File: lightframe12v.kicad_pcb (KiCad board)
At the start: 2 copper layers, 91.4 x 45.7 mm, 47 parts, among them J1 PJ-077, J2 Conn_01x07_Female, J4 Conn_01x07_Female, J5 Conn_01x04_Female, J6 Conn_01x4_Female, Q1 MMBT2222A-TP, Q2 MMBT2222A-TP, SW1 SW_Push, SW2 SW_Push, U1 TPS562211, U2 ESP32-WROOM-32U, U3 TLC5971

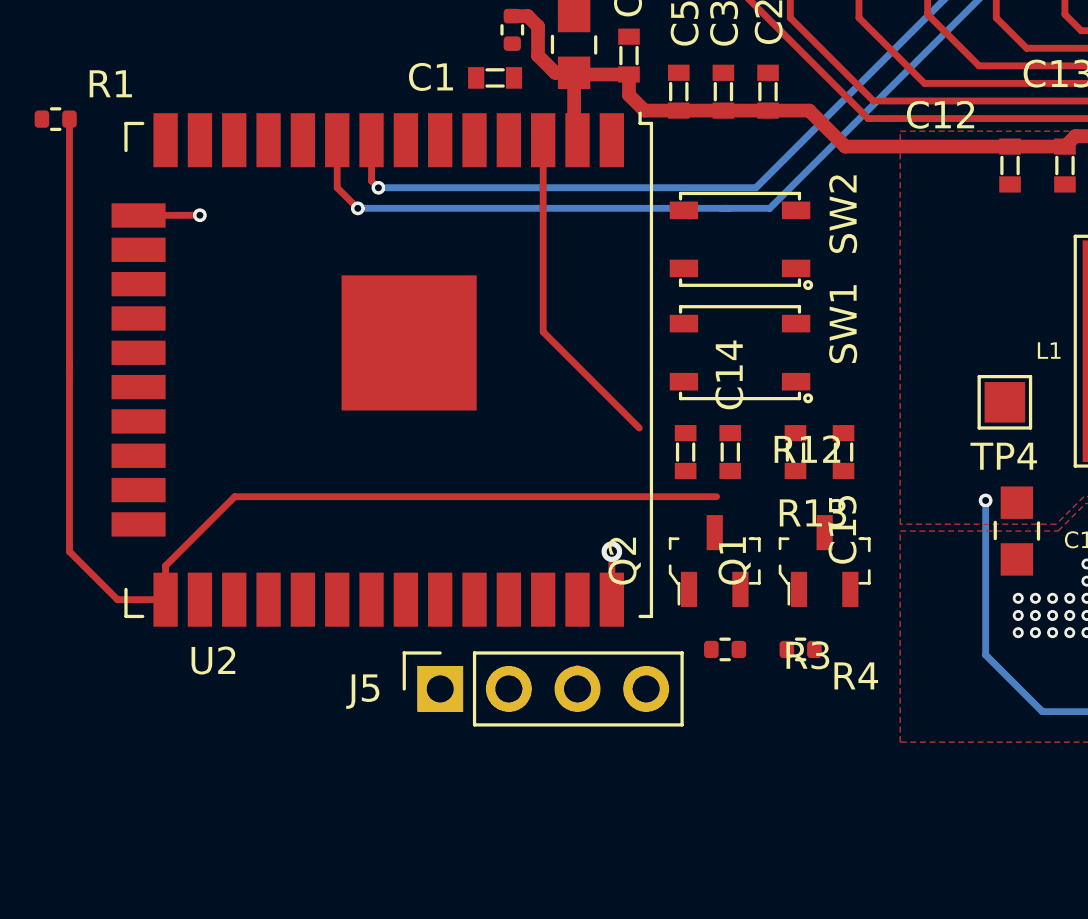
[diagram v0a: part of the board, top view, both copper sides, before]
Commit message: Connecting reset and gpio0.
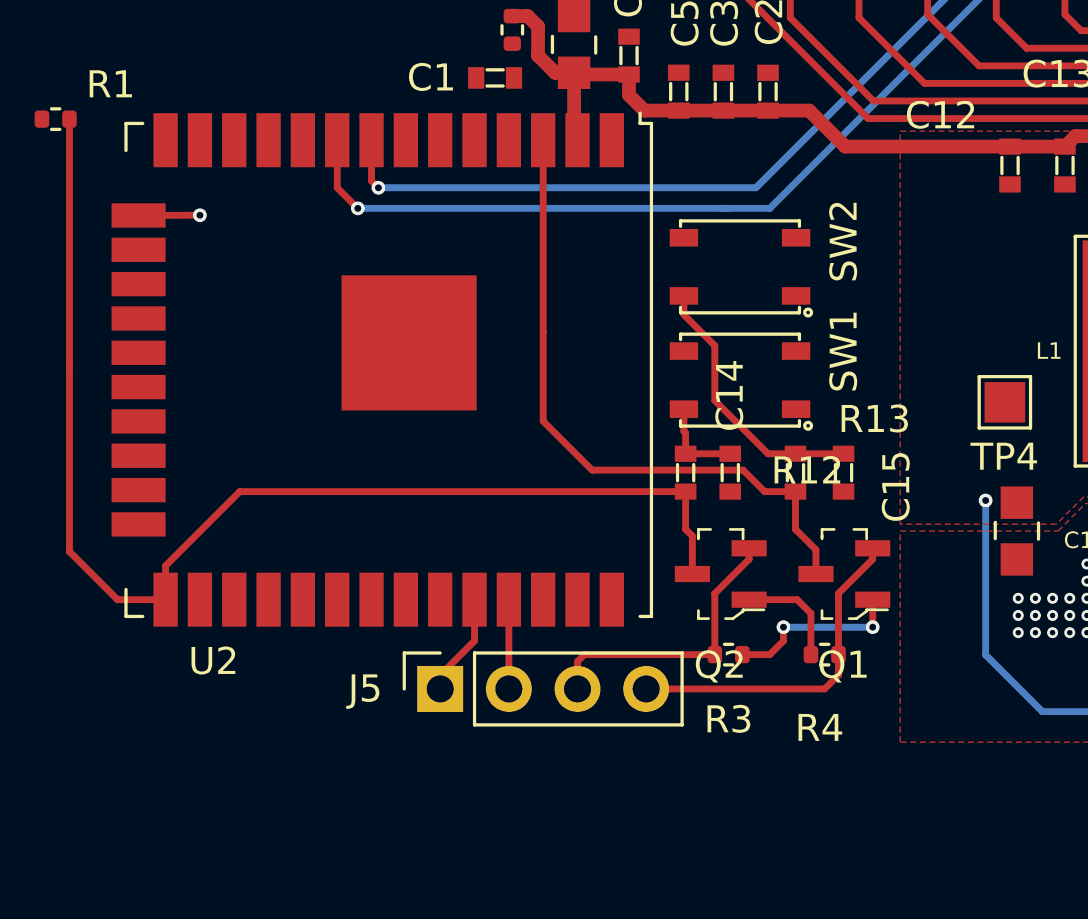
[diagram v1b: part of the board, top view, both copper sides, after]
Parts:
- moved SW2 1.02 mm to (318.9, -523.4)
- moved SW1 1.02 mm to (318.9, -519.2)
- moved R4 0.91 mm to (322.1, -509.0)
- moved Q1 0.87 mm to (322.8, -512.0), turned to 180 degrees
- moved C14 0.76 mm to (318.6, -515.7)
- moved C15 0.76 mm to (322.8, -515.7)
- moved R12 0.76 mm to (316.9, -515.7)
- moved R13 0.76 mm to (321.0, -515.7)
- moved Q2 0.53 mm to (318.2, -512.0), turned to 180 degrees
- moved R3 0.23 mm to (318.5, -509.0)
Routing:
- net /Rts: track 0.00 -> 12.5 mm
- net /Reset: track 12.6 -> 24.6 mm
- net Net-(C15-Pad2): track 0.00 -> 9.92 mm
- net /Dtr: track 0.76 -> 10.7 mm
- net Net-(Q1-Pad1): track 0.00 -> 6.56 mm, vias 0 -> 2
- net Net-(Q2-Pad1): track 0.00 -> 4.02 mm
- net Net-(C14-Pad2): track 0.00 -> 3.33 mm
- net /Rxd: track 0.51 -> 3.83 mm
- net /Txd: track 0.00 -> 3.30 mm
- net /Gpio0: track 43.0 -> 45.1 mm
- net GND: track 6.10 -> 4.32 mm, vias 72 -> 71

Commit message: More routing.
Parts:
- moved R1 23.7 mm to (317.2, -527.6), turned to 270 degrees
- moved T12V 14.7 mm to (355.9, -527.2)
- moved J6 4.13 mm to (299.7, -537.0)
- moved TPG 3.81 mm to (356.1, -508.4)
- moved T3V3 3.78 mm to (327.7, -522.0)
- moved J1 2.87 mm to (354.2, -521.6)
- moved TGND 2.29 mm to (356.1, -511.8)
- moved SW1 2.16 mm to (321.1, -519.2)
- moved SW2 2.16 mm to (321.1, -523.4)
- moved R13 1.53 mm to (322.4, -516.4), turned to 180 degrees
- moved R6 1.48 mm to (314.2, -534.4)
- moved R12 1.20 mm to (317.9, -516.4), turned to 180 degrees
- moved C15 1.06 mm to (323.3, -514.9), turned to 0 degrees
- moved C14 0.92 mm to (318.8, -514.9), turned to 0 degrees
- moved C12 0.76 mm to (328.9, -526.4)
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- renumbered TP1 to T12V, TP4 to T3V3, TP2 to TGND, TP3 to TPG
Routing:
- net /LED1: track 0.00 -> 21.0 mm
- net GND: track 4.32 -> 23.0 mm, vias 71 -> 85
- net /LED2: track 0.00 -> 18.1 mm
- net +12V: track 5.57 -> 21.7 mm, vias 1 -> 2
- net /LED3: track 0.00 -> 15.1 mm
- net /LED4: track 0.00 -> 12.3 mm
- net /Gpio35: track 0.00 -> 9.64 mm
- net /LED5: track 0.00 -> 9.50 mm
- net /Gpio26: track 0.53 -> 9.75 mm
- net /Gpio34: track 0.00 -> 9.12 mm
- net /Gpio27: track 0.00 -> 9.12 mm
- net /Gpio0: track 45.1 -> 36.3 mm
- net /LED6: track 0.00 -> 6.54 mm
- net /Reset: track 24.6 -> 29.4 mm, vias 0 -> 2
- net Net-(R7-Pad2): track 13.9 -> 17.8 mm
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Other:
- board size 91.4 x 45.7 mm -> 64.8 x 35.6 mm
- board text added: "Dtr"
- board text added: "RESET"
- board text added: "Rts"
- board text added: "Rx"
- board text added: "Tx"
- board text added: "ZERO"

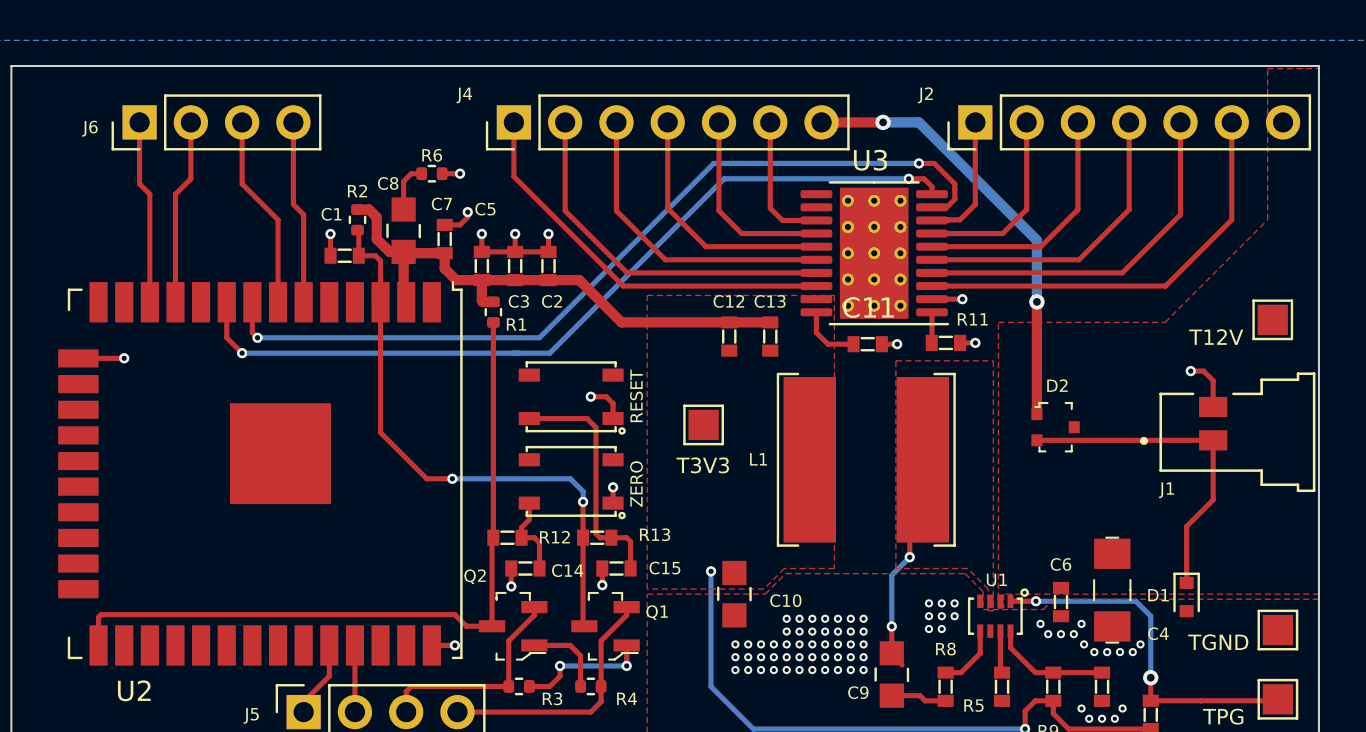
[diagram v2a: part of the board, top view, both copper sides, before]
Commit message: Fixes DRC errors.
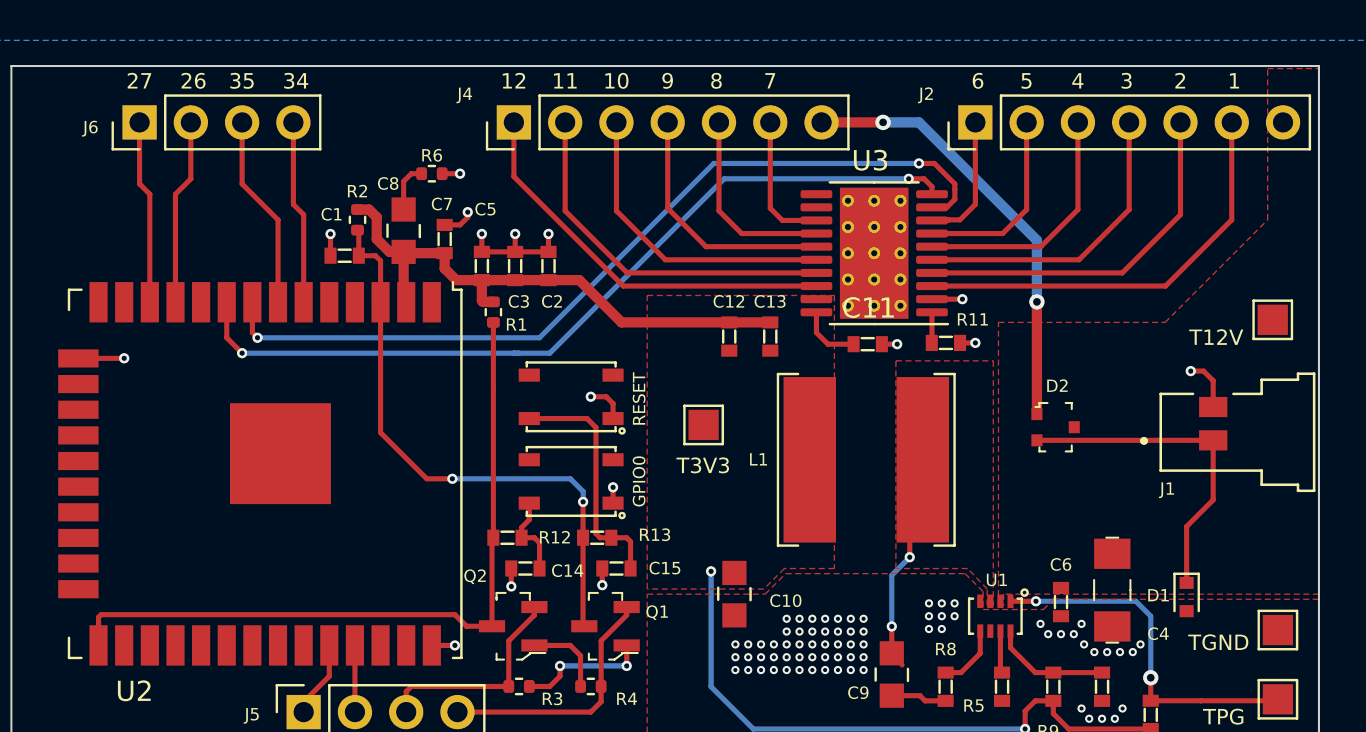
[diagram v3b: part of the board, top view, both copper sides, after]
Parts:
- renumbered SW1 to GPIO0, SW2 to RESET
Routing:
- net (no net): track 0.79 -> 0.00 mm
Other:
- board text added: "1"
- board text added: "10"
- board text added: "11"
- board text added: "12"
- board text added: "2"
- board text added: "26"
- board text added: "27"
- board text added: "3"
- board text added: "34"
- board text added: "35"
- board text added: "4"
- board text added: "5"
- board text added: "6"
- board text added: "7"
- board text added: "8"
- board text added: "9"
- board text removed: "RESET"
- board text removed: "ZERO"

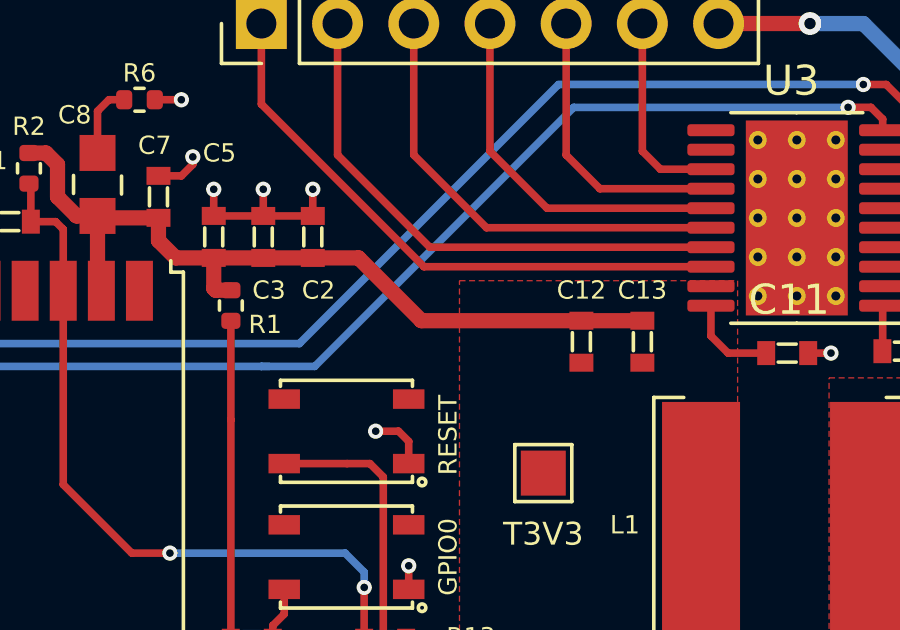
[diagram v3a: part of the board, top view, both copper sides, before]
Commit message: Removes extra thermal pin.
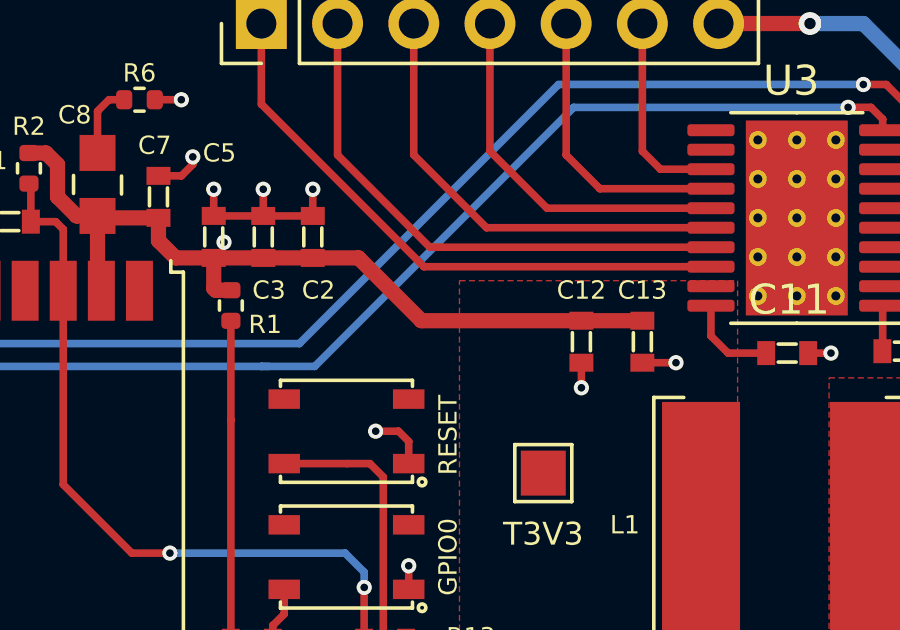
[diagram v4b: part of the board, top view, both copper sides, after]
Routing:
- net GND: track 23.0 -> 25.0 mm, vias 85 -> 87
- net +12V: vias 2 -> 3
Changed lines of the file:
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@@
     (thickness 1.6)
     (drawings 24)
-    (tracks 368)
+    (tracks 375)
     (zones 0)
     (modules 47)
@@
   (segment (start 351.79 -524.637) (end 351.79 -524.637) (width 0.254) (layer F.Cu) (net 1))
   (via (at 351.79 -524.637) (size 0.508) (drill 0.254) (layers F.Cu B.Cu) (net 1))
+  (segment (start 328.93 -525.65) (end 328.93 -524.8148) (width 0.254) (layer F.Cu) (net 1))
+  (segment (start 328.93 -524.8148) (end 328.93 -524.8148) (width 0.254) (layer F.Cu) (net 1))
+  (via (at 328.93 -524.8148) (size 0.508) (drill 0.254) (layers F.Cu B.Cu) (net 1))
+  (segment (start 330.962 -525.65) (end 332.0826 -525.65) (width 0.254) (layer F.Cu) (net 1))
+  (segment (start 332.0826 -525.65) (end 332.0826 -525.65) (width 0.254) (layer F.Cu) (net 1))
+  (via (at 332.0826 -525.65) (size 0.508) (drill 0.254) (layers F.Cu B.Cu) (net 1))
   (segment (start 310.642 -532.64) (end 310.64 -532.638) (width 0.508) (layer F.Cu) (net 2))
   (via (at 343.5858 -506.9078) (size 0.508) (drill 0.254) (layers F.Cu B.Cu) (net 2))
@@
   (segment (start 344.17 -531.114) (end 338.328 -536.956) (width 0.508) (layer B.Cu) (net 33))
   (segment (start 344.17 -528.066) (end 344.17 -531.114) (width 0.508) (layer B.Cu) (net 33))
+  (via (at 317.0174 -529.6662) (size 0.508) (drill 0.254) (layers F.Cu B.Cu) (net 33))
   (segment (start 312.801 -532.6425) (end 312.801 -534.035) (width 0.254) (layer F.Cu) (net 34))
   (segment (start 313.182 -534.416) (end 313.69 -534.416) (width 0.254) (layer F.Cu) (net 34))

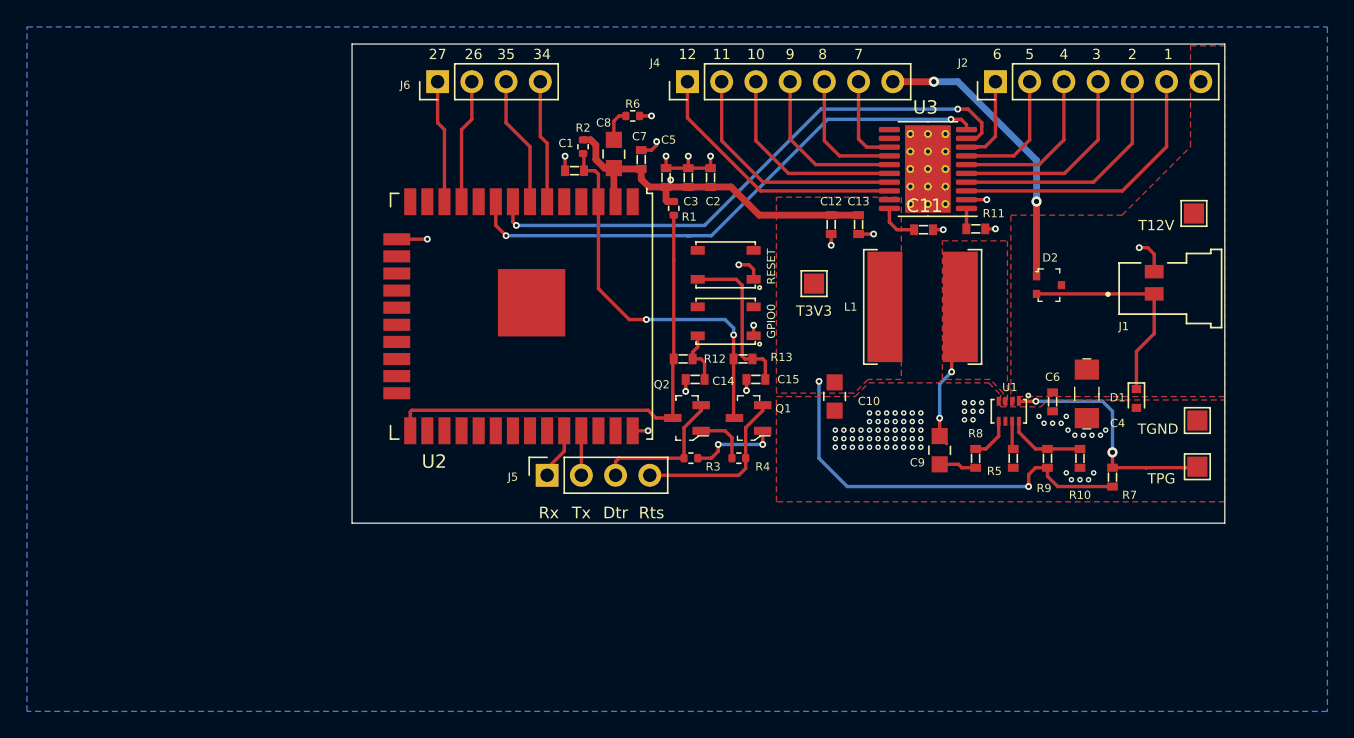
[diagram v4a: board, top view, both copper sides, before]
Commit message: Fiducials and mount points.
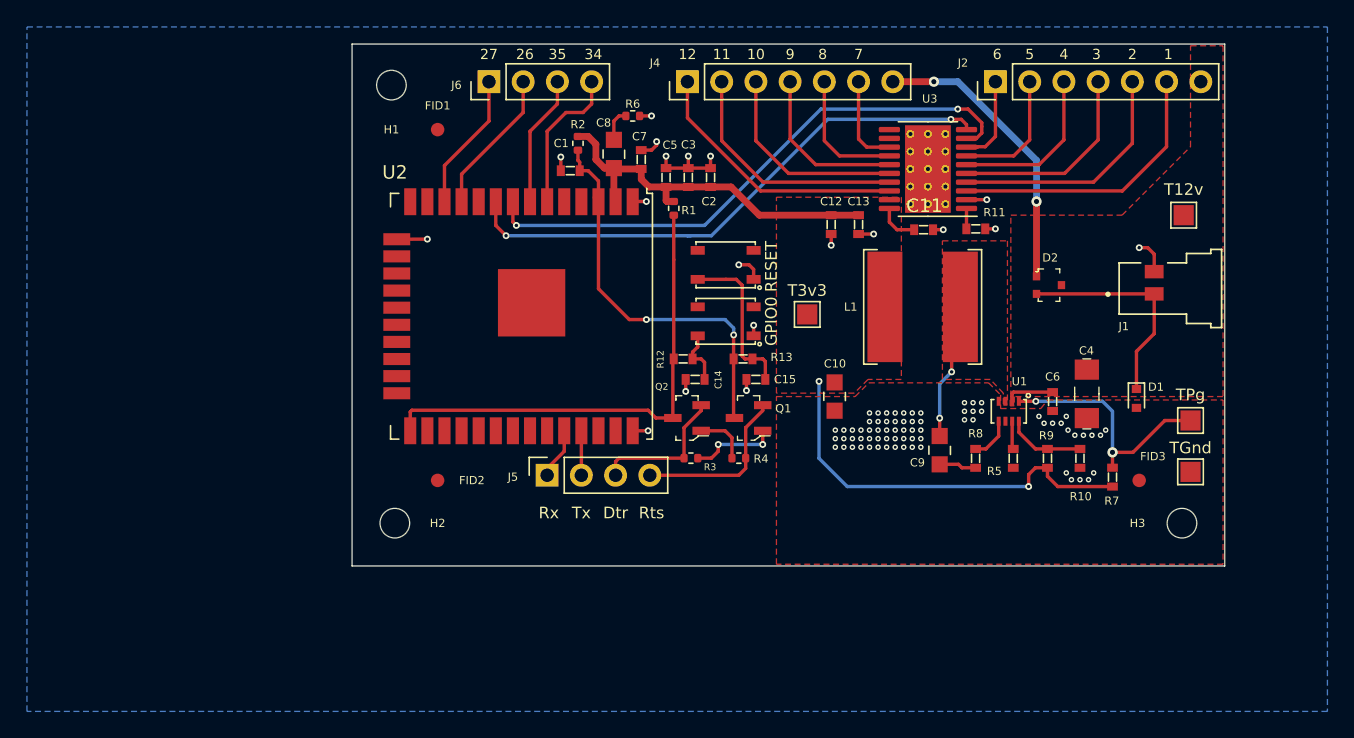
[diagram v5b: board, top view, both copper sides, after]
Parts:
- added FID1: Fiducial, Fiducial:Fiducial_1mm_Mask2mm, F.Cu at (299.7, -533.4)
- added FID2: Fiducial, Fiducial:Fiducial_1mm_Mask2mm, F.Cu at (299.7, -507.4)
- added FID3: Fiducial, Fiducial:Fiducial_1mm_Mask2mm, F.Cu at (351.8, -507.4)
- added H1: TopLeft, MountingHole:MountingHole_2.2mm_M2, F.Cu at (296.3, -536.7)
- added H2: BottomLeft, MountingHole:MountingHole_2.2mm_M2, F.Cu at (296.5, -504.2)
- added H3: TopRight, MountingHole:MountingHole_2.2mm_M2, F.Cu at (355.0, -504.2)
- moved TP2 3.84 mm to (355.6, -508.0)
- moved J6 3.81 mm to (303.5, -537.0)
- moved TP3 3.47 mm to (355.6, -511.8)
- moved TP4 2.34 mm to (327.2, -519.7)
- moved TP1 0.77 mm to (355.1, -527.0)
- moved R2 0.46 mm to (310.1, -532.4)
- moved C1 0.31 mm to (309.6, -530.4)
- renumbered GPIO0 to SW1, RESET to SW2, T12V to TP1, TGND to TP2, TPG to TP3, T3V3 to TP4
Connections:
- U2 pad 39: GND -> (no net)
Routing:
- net +12V: track 21.7 -> 25.3 mm, vias 3 -> 2
- net /Gpio34: track 9.12 -> 11.0 mm
- net /Gpio26: track 9.75 -> 11.3 mm
- net /Gpio27: track 9.12 -> 10.3 mm
- net GND: track 25.0 -> 25.9 mm, vias 87 -> 88
- net +3V3: track 58.5 -> 59.0 mm
- added copper zone on B.Cu, net GND
- removed copper zone on B.Cu, net +12V
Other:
- board size 64.8 x 35.6 mm -> 64.8 x 38.7 mm
- board text added: "GPIO0"
- board text added: "RESET"
- board text added: "T12v"
- board text added: "T3v3"
- board text added: "TGnd"
- board text added: "TPg"

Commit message: Spaced out.
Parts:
- moved TP2 16.5 mm to (339.9, -502.9)
- moved TP3 15.1 mm to (343.4, -502.9)
- moved J5 3.56 mm to (307.8, -504.2)
- moved R7 2.34 mm to (349.2, -505.3), turned to 0 degrees
- moved D1 0.71 mm to (352.3, -513.4)
- moved R10 0.62 mm to (347.4, -508.4)
- moved C2 0.57 mm to (320.5, -529.8)
- moved C4 0.48 mm to (348.1, -513.4)
- moved C3 0.32 mm to (318.6, -529.8)
- moved C5 0.06 mm to (316.7, -529.8)
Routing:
- net Net-(R7-Pad2): track 18.2 -> 24.4 mm
- net /Txd: track 3.30 -> 7.11 mm
- net /Rts: track 12.5 -> 16.2 mm
- net /Rxd: track 3.83 -> 7.38 mm
- net /Dtr: track 10.7 -> 14.1 mm
- net GND: track 25.9 -> 28.2 mm, vias 88 -> 76
- net +3V3: track 59.0 -> 59.6 mm
- net /LED4: track 12.3 -> 12.8 mm
- net (no net): vias 2 -> 0
